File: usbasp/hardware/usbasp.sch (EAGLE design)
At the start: 25 parts, among them IC1 ATMEGA8-16A, Q2 12Mhz, X1 USB-A-H

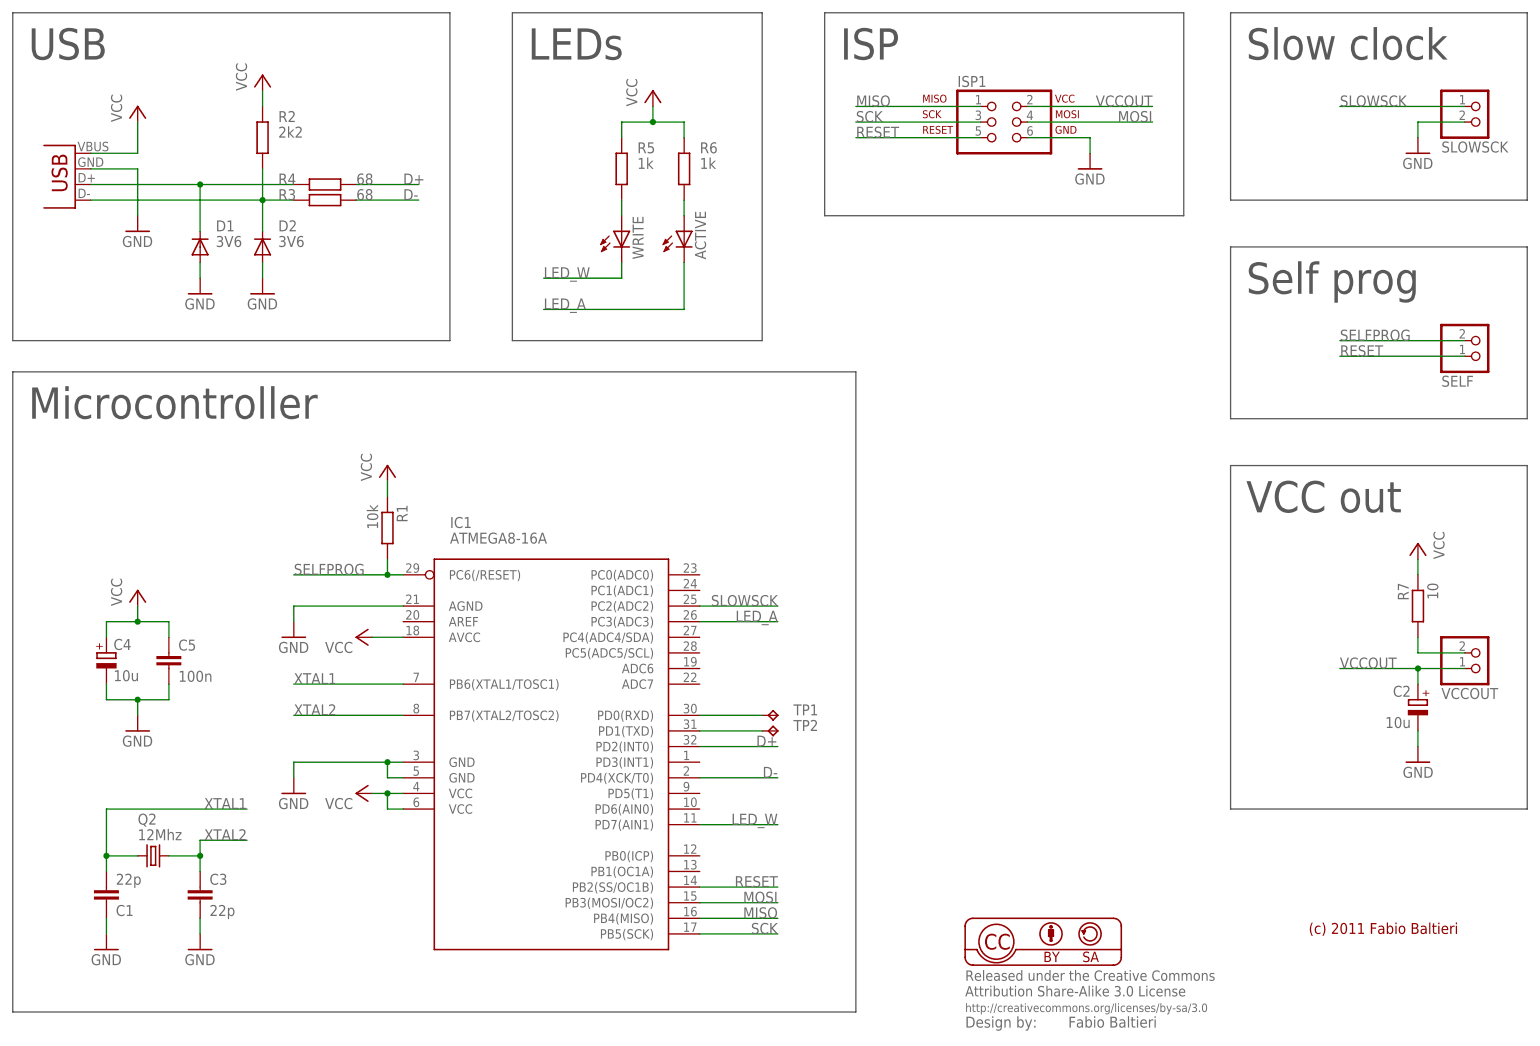
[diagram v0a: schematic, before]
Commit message: added usbtiny + many updates
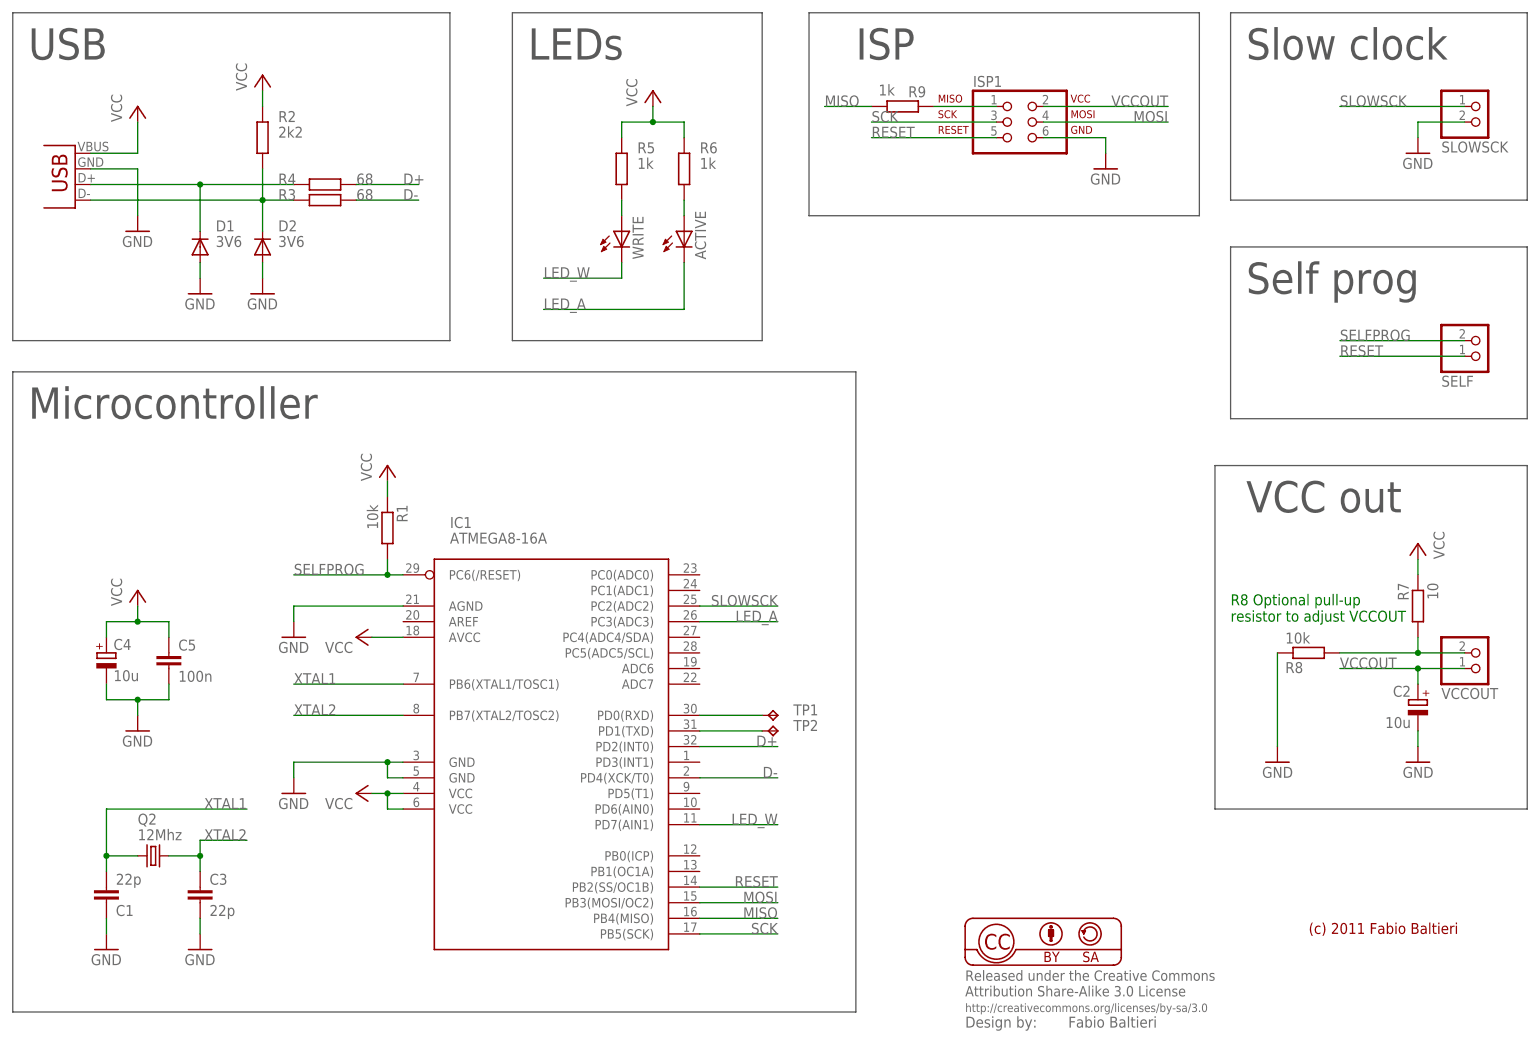
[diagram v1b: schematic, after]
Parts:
- added R8: 10k, rcl:R-EU_M0805
- added R9: 1k, rcl:R-EU_M0805
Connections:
- new net N$1: ISP1.1, R9.1
- net GND: now also R8.1
- net MISO: now also R9.2; no longer ISP1.1
- net N$11: now also R8.2
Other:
- note added: "R8 Optional pull-up resistor to adjust VCCOUT"
- moved on the sheet: ISP1
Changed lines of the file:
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@@
 <part name="GND9" library="supply1" deviceset="GND" device=""/>
 <part name="GND11" library="supply1" deviceset="GND" device=""/>
+<part name="R8" library="rcl" deviceset="R-EU_" device="M0805" value="10k"/>
+<part name="GND12" library="supply1" deviceset="GND" device=""/>
+<part name="R9" library="rcl" deviceset="R-EU_" device="M0805" value="1k"/>
 </parts>
 <sheets>
@@
 <text x="10.16" y="162.56" size="5.08" layer="97">USB</text>
 <text x="91.44" y="162.56" size="5.08" layer="97">LEDs</text>
-<wire x1="139.7" y1="170.18" x2="198.12" y2="170.18" width="0.1524" layer="97"/>
-<wire x1="198.12" y1="170.18" x2="198.12" y2="137.16" width="0.1524" layer="97"/>
-<wire x1="198.12" y1="137.16" x2="139.7" y2="137.16" width="0.1524" layer="97"/>
-<wire x1="139.7" y1="137.16" x2="139.7" y2="170.18" width="0.1524" layer="97"/>
-<text x="142.24" y="162.56" size="5.08" layer="97">ISP</text>
+<wire x1="137.16" y1="170.18" x2="200.66" y2="170.18" width="0.1524" layer="97"/>
+<wire x1="200.66" y1="170.18" x2="200.66" y2="137.16" width="0.1524" layer="97"/>
+<wire x1="200.66" y1="137.16" x2="137.16" y2="137.16" width="0.1524" layer="97"/>
+<wire x1="137.16" y1="137.16" x2="137.16" y2="170.18" width="0.1524" layer="97"/>
+<text x="144.78" y="162.56" size="5.08" layer="97">ISP</text>
 <text x="208.28" y="162.56" size="5.08" layer="97">Slow clock</text>
 <text x="208.28" y="124.46" size="5.08" layer="97">Self prog</text>
@@
 <wire x1="205.74" y1="104.14" x2="205.74" y2="132.08" width="0.1524" layer="97"/>
 <wire x1="205.74" y1="132.08" x2="254" y2="132.08" width="0.1524" layer="97"/>
-<wire x1="205.74" y1="96.52" x2="254" y2="96.52" width="0.1524" layer="97"/>
+<wire x1="203.2" y1="96.52" x2="254" y2="96.52" width="0.1524" layer="97"/>
 <wire x1="254" y1="96.52" x2="254" y2="40.64" width="0.1524" layer="97"/>
-<wire x1="254" y1="40.64" x2="205.74" y2="40.64" width="0.1524" layer="97"/>
-<wire x1="205.74" y1="40.64" x2="205.74" y2="96.52" width="0.1524" layer="97"/>
+<wire x1="254" y1="40.64" x2="203.2" y2="40.64" width="0.1524" layer="97"/>
+<wire x1="203.2" y1="40.64" x2="203.2" y2="96.52" width="0.1524" layer="97"/>
+<text x="205.74" y="71.12" size="1.778" layer="91">R8 Optional pull-up
+resistor to adjust VCCOUT</text>
 </plain>
 <instances>
@@
 <attribute name="VALUE" x="240.03" y="121.92" size="1.778" layer="96" rot="MR180"/>
 </instance>
-<instance part="GND8" gate="1" x="182.88" y="144.78" smashed="yes">
-<attribute name="VALUE" x="180.34" y="142.24" size="1.778" layer="96"/>
+<instance part="GND8" gate="1" x="185.42" y="144.78" smashed="yes">
+<attribute name="VALUE" x="182.88" y="142.24" size="1.778" layer="96"/>
 </instance>
 <instance part="GND10" gate="1" x="236.22" y="48.26" smashed="yes" rot="MR0">
@@
 </instance>
 <instance part="X1" gate="G$1" x="17.78" y="147.32" smashed="yes" rot="R180"/>
-<instance part="ISP1" gate="A" x="167.64" y="152.4" smashed="yes">
-<attribute name="NAME" x="161.29" y="158.115" size="1.778" layer="95"/>
-<attribute name="VALUE" x="161.29" y="144.78" size="1.778" layer="96"/>
+<instance part="ISP1" gate="A" x="170.18" y="152.4" smashed="yes">
+<attribute name="NAME" x="163.83" y="158.115" size="1.778" layer="95"/>
+<attribute name="VALUE" x="163.83" y="144.78" size="1.778" layer="96"/>
 </instance>
 <instance part="TP1" gate="G$1" x="132.08" y="55.88" smashed="yes" rot="R270">
@@
 <instance part="GND11" gate="1" x="22.86" y="17.78" smashed="yes">
 <attribute name="VALUE" x="20.32" y="15.24" size="1.778" layer="96"/>
+</instance>
+<instance part="R8" gate="G$1" x="218.44" y="66.04" smashed="yes" rot="MR180">
+<attribute name="NAME" x="214.63" y="64.5414" size="1.778" layer="95" rot="MR180"/>
+<attribute name="VALUE" x="214.63" y="69.342" size="1.778" layer="96" rot="MR180"/>
+</instance>
+<instance part="GND12" gate="1" x="213.36" y="48.26" smashed="yes" rot="MR0">
+<attribute name="VALUE" x="215.9" y="45.72" size="1.778" layer="96" rot="MR0"/>
+</instance>
+<instance part="R9" gate="G$1" x="152.4" y="154.94" smashed="yes" rot="MR0">
+<attribute name="NAME" x="156.21" y="156.4386" size="1.778" layer="95" rot="MR0"/>
+<attribute name="VALUE" x="151.13" y="156.718" size="1.778" layer="96" rot="MR0"/>
 </instance>
 </instances>
@@
 </segment>
 <segment>
-<wire x1="172.72" y1="149.86" x2="182.88" y2="149.86" width="0.1524" layer="91"/>
-<wire x1="182.88" y1="149.86" x2="182.88" y2="147.32" width="0.1524" layer="91"/>
+<wire x1="175.26" y1="149.86" x2="185.42" y2="149.86" width="0.1524" layer="91"/>
+<wire x1="185.42" y1="149.86" x2="185.42" y2="147.32" width="0.1524" layer="91"/>
 <pinref part="GND8" gate="1" pin="GND"/>
 <pinref part="ISP1" gate="A" pin="6"/>
@@
 <pinref part="GND11" gate="1" pin="GND"/>
 <wire x1="22.86" y1="20.32" x2="22.86" y2="22.86" width="0.1524" layer="91"/>
+</segment>
+<segment>
+<pinref part="R8" gate="G$1" pin="1"/>
+<pinref part="GND12" gate="1" pin="GND"/>
+<wire x1="213.36" y1="66.04" x2="213.36" y2="50.8" width="0.1524" layer="91"/>
 </segment>
 </net>
@@
 </segment>
 <segment>
-<wire x1="172.72" y1="154.94" x2="193.04" y2="154.94" width="0.1524" layer="91"/>
-<label x="193.04" y="154.94" size="1.778" layer="95" rot="MR0"/>
+<wire x1="175.26" y1="154.94" x2="195.58" y2="154.94" width="0.1524" layer="91"/>
+<label x="195.58" y="154.94" size="1.778" layer="95" rot="MR0"/>
 <pinref part="ISP1" gate="A" pin="2"/>
 </segment>
@@
 </segment>
 <segment>
-<wire x1="172.72" y1="152.4" x2="193.04" y2="152.4" width="0.1524" layer="91"/>
-<label x="193.04" y="152.4" size="1.778" layer="95" rot="MR0"/>
+<wire x1="175.26" y1="152.4" x2="195.58" y2="152.4" width="0.1524" layer="91"/>
+<label x="195.58" y="152.4" size="1.778" layer="95" rot="MR0"/>
 <pinref part="ISP1" gate="A" pin="4"/>
 </segment>
@@
 </segment>
 <segment>
-<wire x1="165.1" y1="154.94" x2="144.78" y2="154.94" width="0.1524" layer="91"/>
-<label x="144.78" y="154.94" size="1.778" layer="95"/>
-<pinref part="ISP1" gate="A" pin="1"/>
+<wire x1="147.32" y1="154.94" x2="139.7" y2="154.94" width="0.1524" layer="91"/>
+<pinref part="R9" gate="G$1" pin="2"/>
+<label x="139.7" y="154.94" size="1.778" layer="95"/>
 </segment>
 </net>
@@
 </segment>
 <segment>
-<wire x1="165.1" y1="152.4" x2="144.78" y2="152.4" width="0.1524" layer="91"/>
-<label x="144.78" y="152.4" size="1.778" layer="95"/>
+<wire x1="167.64" y1="152.4" x2="147.32" y2="152.4" width="0.1524" layer="91"/>
+<label x="147.32" y="152.4" size="1.778" layer="95"/>
 <pinref part="ISP1" gate="A" pin="3"/>
 </segment>
@@
 </segment>
 <segment>
-<wire x1="165.1" y1="149.86" x2="144.78" y2="149.86" width="0.1524" layer="91"/>
-<label x="144.78" y="149.86" size="1.778" layer="95"/>
+<wire x1="167.64" y1="149.86" x2="147.32" y2="149.86" width="0.1524" layer="91"/>
+<label x="147.32" y="149.86" size="1.778" layer="95"/>
 <pinref part="ISP1" gate="A" pin="5"/>
 </segment>
@@
 <pinref part="R7" gate="G$1" pin="2"/>
 <pinref part="VCCOUT" gate="G$1" pin="2"/>
+<pinref part="R8" gate="G$1" pin="2"/>
+<wire x1="223.52" y1="66.04" x2="236.22" y2="66.04" width="0.1524" layer="91"/>
+<junction x="236.22" y="66.04"/>
 </segment>
 </net>
@@
 <pinref part="IC1" gate="G$1" pin="PD1(TXD)"/>
 <pinref part="TP2" gate="G$1" pin="TP"/>
+</segment>
+</net>
+<net name="N$1" class="0">
+<segment>
+<pinref part="R9" gate="G$1" pin="1"/>
+<pinref part="ISP1" gate="A" pin="1"/>
+<wire x1="157.48" y1="154.94" x2="167.64" y2="154.94" width="0.1524" layer="91"/>
 </segment>
 </net>
@@
 </schematic>
 </drawing>
+<compatibility>
+<note version="6.3" minversion="6.2.2" severity="warning">
+Since Version 6.2.2 text objects can contain more than one line,
+which will not be processed correctly with this version.
+</note>
+</compatibility>
 </eagle>

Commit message: lots of updates
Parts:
- removed R8: 10k, rcl:R-EU_M0805
- removed R9: 1k, rcl:R-EU_M0805
- added LED1, LED2: (no value), led:LEDCHIP-LED0805
- R7: value 10 -> 10R
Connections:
- removed net N$1: ISP1.1, R9.1
- net GND: now also LED1.C, LED2.C; no longer R8.1
- net MISO: now also ISP1.1; no longer R9.2
- net N$11: no longer R8.2
- net N$6: now also LED1.A
- net N$7: now also LED2.A
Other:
- note added: "Zener Diodes or LED to GND"
- note removed: "R8 Optional pull-up resistor to adjust VCCOUT"
- moved on the sheet: D2, R2, R3, R4
